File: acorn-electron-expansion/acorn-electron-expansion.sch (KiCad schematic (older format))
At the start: 11 parts, among them P1 Acorn Electron Expansion Conn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, P2 CONN_02X24, U1 74hct125d, U2 74LVC245 D0-7, U3 74LVC245 A0-7, U4 74LVC245 A8-15, U5 74LVC245

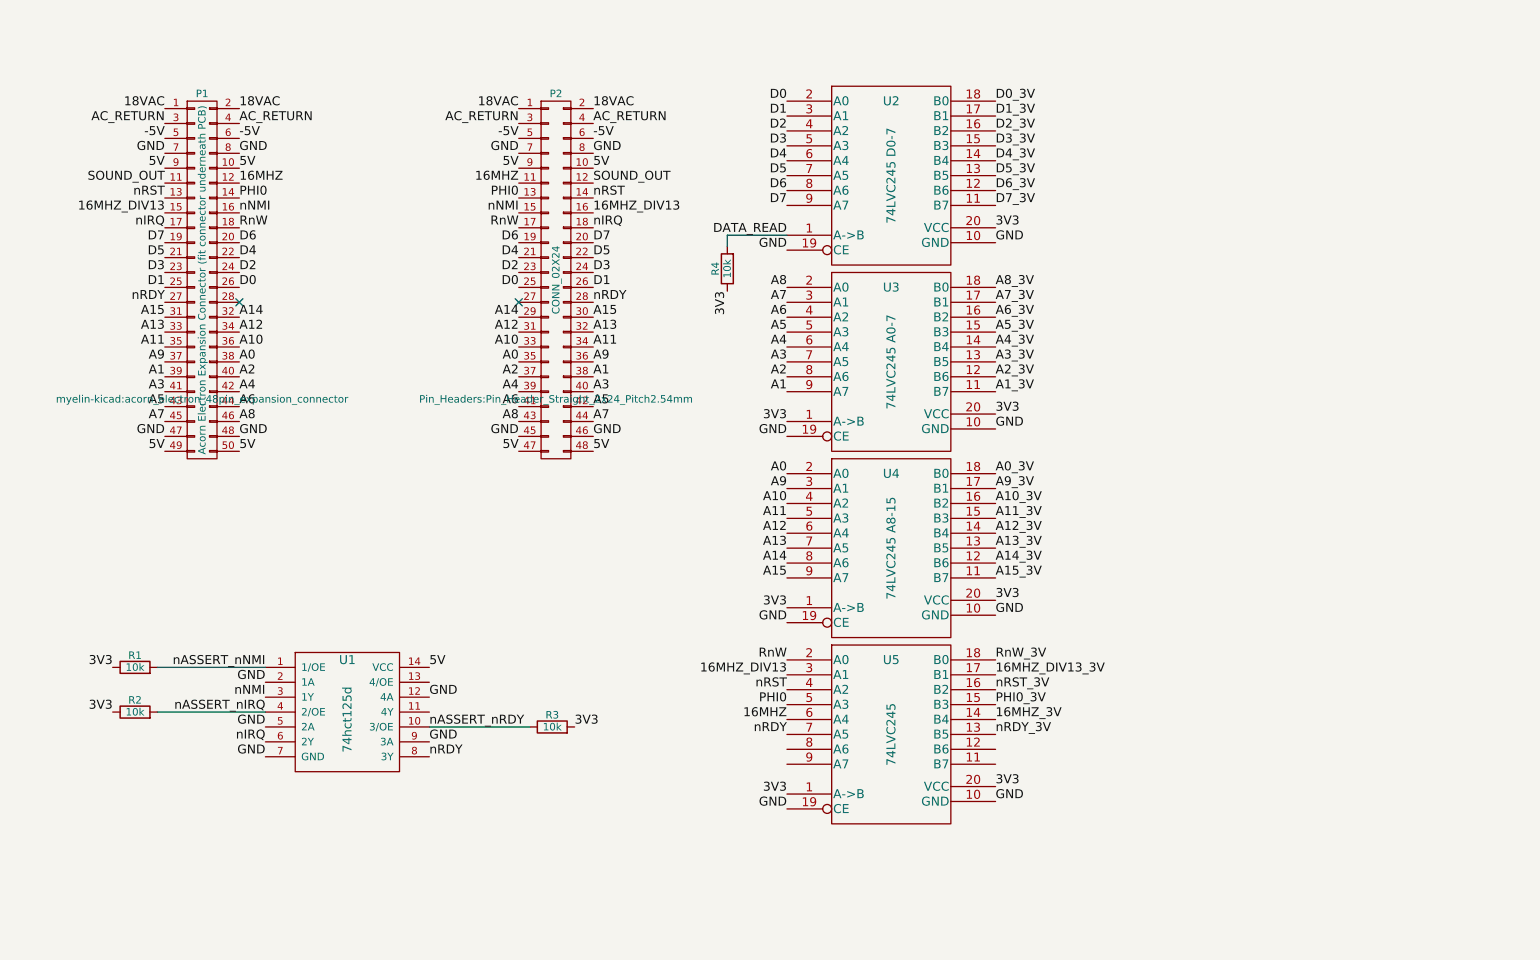
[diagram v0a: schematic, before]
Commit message: Made library and module for Scarab miniSpartan6+ board, and routed most of the level conversion stuff up top
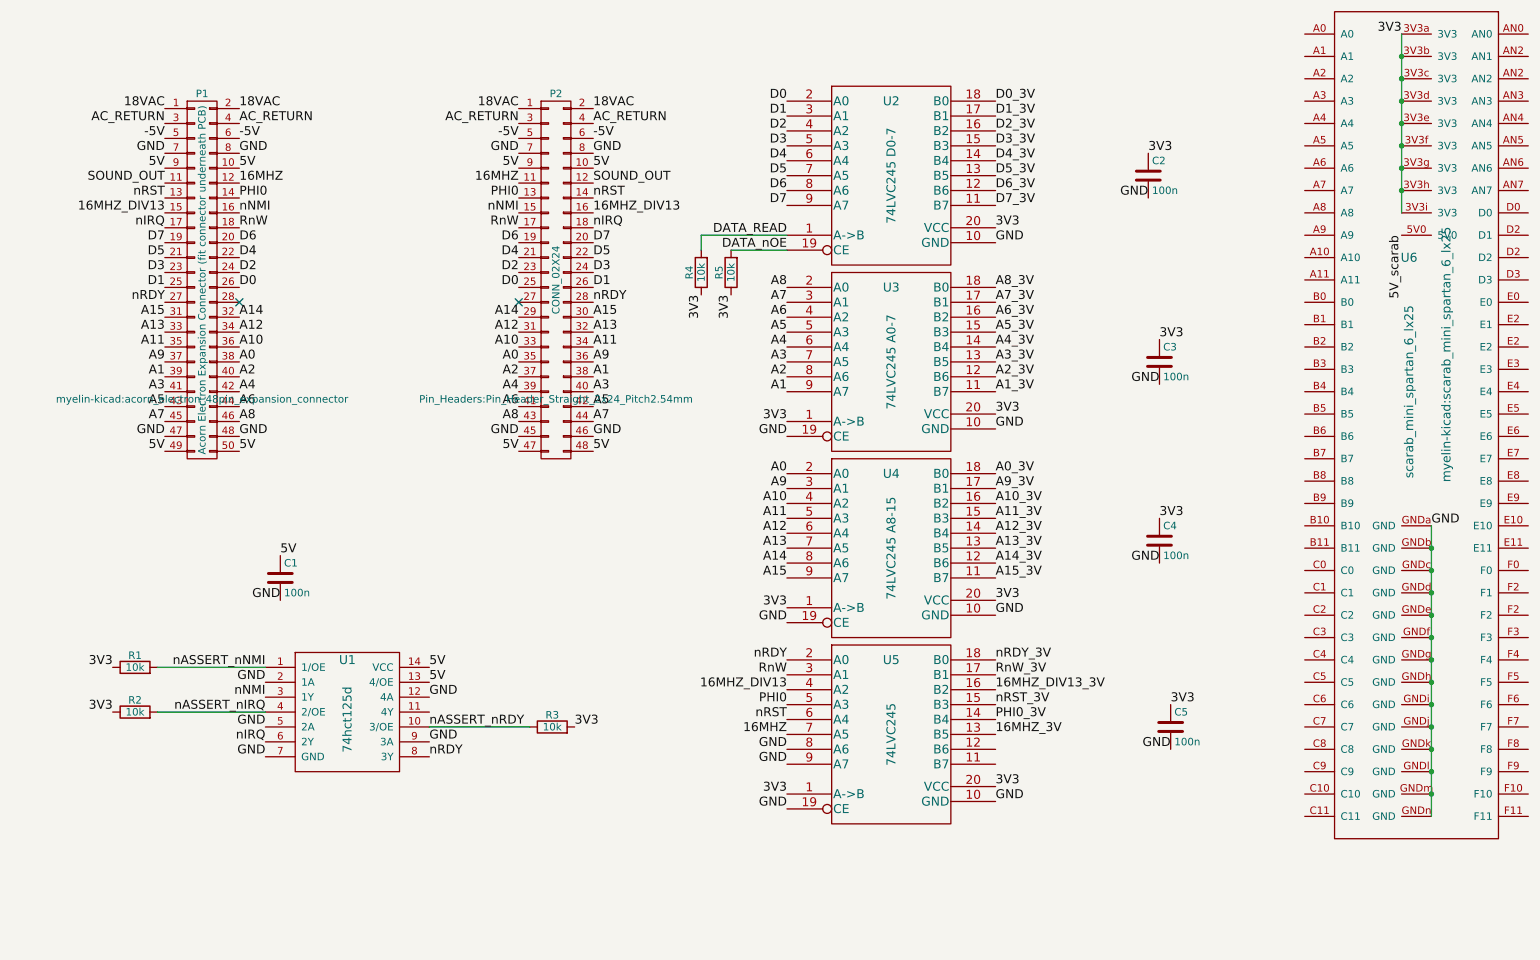
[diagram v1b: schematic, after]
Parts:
- added C1, C2, C3, C4, C5: 100n, myelin-kicad:C0805_nosilkscreen, symbol C0805
- added R5: 10k, myelin-kicad:R0805_nosilkscreen, symbol R0805
- added U6: scarab_mini_spartan_6_lx25, myelin-kicad:scarab_mini_spartan_6_lx25, symbol scarab_mini_spartan_6_lx25
- U2, U3, U4, U5: footprint Housings_SOIC:SOIC-20W_7.5x12.8mm_Pitch1.27mm -> Housings_SSOP:SSOP-20_4.4x6.5mm_Pitch0.65mm
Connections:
- net 16MHZ: now also U5.7 (A5); no longer U5.6 (A4)
- net 16MHZ_3V: now also U5.13 (B5); no longer U5.14 (B4)
- net 16MHZ_DIV13: now also U5.4 (A2); no longer U5.3 (A1)
- net 16MHZ_DIV13_3V: now also U5.16 (B2); no longer U5.17 (B1)
- net 3V3: now also C2.1, C3.1, C4.1, C5.1, R5.1, U6.3V3a (3V3), U6.3V3b (3V3), U6.3V3c (3V3), U6.3V3d (3V3), U6.3V3e (3V3), U6.3V3f (3V3), U6.3V3g (3V3), U6.3V3h (3V3), U6.3V3i (3V3)
- net 5V: now also U1.13 (4/OE), C1.1
- net GND: now also U5.8 (A6), U5.9 (A7), C1.2, C2.2, C3.2, C4.2, C5.2, U6.GNDa (GND), U6.GNDb (GND), U6.GNDc (GND), U6.GNDd (GND), U6.GNDe (GND), U6.GNDf (GND), U6.GNDg (GND), U6.GNDh (GND), U6.GNDi (GND), U6.GNDj (GND), U6.GNDk (GND), U6.GNDl (GND), U6.GNDm (GND), U6.GNDn (GND); no longer U2.19 (CE)
- net PHI0_3V: now also U5.14 (B4); no longer U5.15 (B3)
- net RnW: now also U5.3 (A1); no longer U5.2 (A0)
- net RnW_3V: now also U5.17 (B1); no longer U5.18 (B0)
- net nRDY: now also U5.2 (A0); no longer U5.7 (A5)
- net nRDY_3V: now also U5.18 (B0); no longer U5.13 (B5)
- net nRST: now also U5.6 (A4); no longer U5.4 (A2)
- net nRST_3V: now also U5.15 (B3); no longer U5.16 (B2)
- new net 5V_scarab: U6.5V0
- new net DATA_nOE: R5.2, U2.19 (CE)
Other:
- moved on the sheet: R4
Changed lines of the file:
@@
 LIBS:c0805
 LIBS:r0805
+LIBS:scarab_mini_spartan_6_lx25
+LIBS:acorn-electron-expansion-cache
 EELAYER 25 0
 EELAYER END
@@
 F 0 "U2" H 6300 2250 60  0000 C CNN
 F 1 "74LVC245 D0-7" V 6300 1750 60  0000 C CNN
-F 2 "Housings_SOIC:SOIC-20W_7.5x12.8mm_Pitch1.27mm" H 6300 1050 60  0001 C CNN
+F 2 "Housings_SSOP:SSOP-20_4.4x6.5mm_Pitch0.65mm" H 6300 1050 60  0001 C CNN
 F 3 "" H 6300 1750 60  0000 C CNN
 	1    6300 1750
@@
 F 0 "U3" H 6300 3500 60  0000 C CNN
 F 1 "74LVC245 A0-7" V 6300 3000 60  0000 C CNN
-F 2 "Housings_SOIC:SOIC-20W_7.5x12.8mm_Pitch1.27mm" H 6300 2300 60  0001 C CNN
+F 2 "Housings_SSOP:SSOP-20_4.4x6.5mm_Pitch0.65mm" H 6300 2300 60  0001 C CNN
 F 3 "" H 6300 3000 60  0000 C CNN
 	1    6300 3000
@@
 F 0 "U4" H 6300 4750 60  0000 C CNN
 F 1 "74LVC245 A8-15" V 6300 4250 60  0000 C CNN
-F 2 "Housings_SOIC:SOIC-20W_7.5x12.8mm_Pitch1.27mm" H 6300 3550 60  0001 C CNN
+F 2 "Housings_SSOP:SSOP-20_4.4x6.5mm_Pitch0.65mm" H 6300 3550 60  0001 C CNN
 F 3 "" H 6300 4250 60  0000 C CNN
 	1    6300 4250
@@
 F 0 "U5" H 6300 6000 60  0000 C CNN
 F 1 "74LVC245" V 6300 5500 60  0000 C CNN
-F 2 "Housings_SOIC:SOIC-20W_7.5x12.8mm_Pitch1.27mm" H 6300 4800 60  0001 C CNN
+F 2 "Housings_SSOP:SSOP-20_4.4x6.5mm_Pitch0.65mm" H 6300 4800 60  0001 C CNN
 F 3 "" H 6300 5500 60  0000 C CNN
 	1    6300 5500
@@
 Text Label 5600 4450 2    60   ~ 0
 A15
-Text Label 5600 5400 2    60   ~ 0
+Text Label 5600 5500 2    60   ~ 0
 16MHZ
 Text Label 5600 5300 2    60   ~ 0
 PHI0
+Text Label 5600 5200 2    60   ~ 0
+16MHZ_DIV13
 Text Label 5600 5100 2    60   ~ 0
-16MHZ_DIV13
-Text Label 5600 5000 2    60   ~ 0
 RnW
-Text Label 5600 5200 2    60   ~ 0
+Text Label 5600 5400 2    60   ~ 0
 nRST
 Text Label 2100 5250 2    60   ~ 0
@@
 Text Label 5600 6000 2    60   ~ 0
 GND
-Text Label 7000 5000 0    60   ~ 0
+Text Label 7000 5100 0    60   ~ 0
 RnW_3V
-Text Label 7000 5100 0    60   ~ 0
+Text Label 7000 5200 0    60   ~ 0
 16MHZ_DIV13_3V
-Text Label 7000 5200 0    60   ~ 0
+Text Label 7000 5300 0    60   ~ 0
 nRST_3V
-Text Label 7000 5300 0    60   ~ 0
+Text Label 7000 5400 0    60   ~ 0
 PHI0_3V
-Text Label 7000 5400 0    60   ~ 0
+Text Label 7000 5500 0    60   ~ 0
 16MHZ_3V
 Text Label 5600 5900 2    60   ~ 0
@@
 Text Label 5600 3400 2    60   ~ 0
 3V3
-Text Label 5600 2250 2    60   ~ 0
-GND
 $Comp
 L R0805 R4
 U 1 1 58D0D6B7
-P 5200 2375
-F 0 "R4" V 5280 2375 50  0000 C CNN
-F 1 "10k" V 5200 2375 50  0000 C CNN
-F 2 "myelin-kicad:R0805_nosilkscreen" V 5130 2375 50  0001 C CNN
-F 3 "" H 5200 2375 50  0000 C CNN
-	1    5200 2375
+P 5025 2400
+F 0 "R4" V 5105 2400 50  0000 C CNN
+F 1 "10k" V 5025 2400 50  0000 C CNN
+F 2 "myelin-kicad:R0805_nosilkscreen" V 4955 2400 50  0001 C CNN
+F 3 "" H 5025 2400 50  0000 C CNN
+	1    5025 2400
 	-1   0    0    1
 $EndComp
 Text Label 5600 2150 2    60   ~ 0
 DATA_READ
-Text Label 5200 2525 3    60   ~ 0
-3V3
-Wire Wire Line
-	5200 2225 5200 2150
-Wire Wire Line
-	5200 2150 5600 2150
+Text Label 5025 2550 3    60   ~ 0
+3V3
+Wire Wire Line
+	5025 2150 5600 2150
 Text Label 2100 5050 2    60   ~ 0
 nASSERT_nNMI
@@
 Text Label 4175 5450 0    60   ~ 0
 3V3
-Text Label 5600 5500 2    60   ~ 0
+Text Label 5600 5000 2    60   ~ 0
 nRDY
-Text Label 7000 5500 0    60   ~ 0
+Text Label 7000 5000 0    60   ~ 0
 nRDY_3V
+Text Label 5600 5600 2    60   ~ 0
+GND
+Text Label 5600 5700 2    60   ~ 0
+GND
+Text Label 3200 5150 0    60   ~ 0
+5V
+$Comp
+L C0805 C1
+U 1 1 58D21967
+P 2200 4450
+F 0 "C1" H 2225 4550 50  0000 L CNN
+F 1 "100n" H 2225 4350 50  0000 L CNN
+F 2 "myelin-kicad:C0805_nosilkscreen" H 2238 4300 50  0001 C CNN
+F 3 "" H 2200 4450 50  0000 C CNN
+	1    2200 4450
+	1    0    0    -1
+$EndComp
+Text Label 2200 4300 0    60   ~ 0
+5V
+Text Label 2200 4600 2    60   ~ 0
+GND
+Text Label 8025 1600 0    60   ~ 0
+3V3
+$Comp
+L C0805 C2
+U 1 1 58D21AC9
+P 8025 1750
+F 0 "C2" H 8050 1850 50  0000 L CNN
+F 1 "100n" H 8050 1650 50  0000 L CNN
+F 2 "myelin-kicad:C0805_nosilkscreen" H 8063 1600 50  0001 C CNN
+F 3 "" H 8025 1750 50  0000 C CNN
+	1    8025 1750
+	1    0    0    -1
+$EndComp
+Text Label 8025 1900 2    60   ~ 0
+GND
+Text Label 8100 2850 0    60   ~ 0
+3V3
+$Comp
+L C0805 C3
+U 1 1 58D21BC6
+P 8100 3000
+F 0 "C3" H 8125 3100 50  0000 L CNN
+F 1 "100n" H 8125 2900 50  0000 L CNN
+F 2 "myelin-kicad:C0805_nosilkscreen" H 8138 2850 50  0001 C CNN
+F 3 "" H 8100 3000 50  0000 C CNN
+	1    8100 3000
+	1    0    0    -1
+$EndComp
+Text Label 8100 3150 2    60   ~ 0
+GND
+Text Label 8100 4050 0    60   ~ 0
+3V3
+$Comp
+L C0805 C4
+U 1 1 58D21C56
+P 8100 4200
+F 0 "C4" H 8125 4300 50  0000 L CNN
+F 1 "100n" H 8125 4100 50  0000 L CNN
+F 2 "myelin-kicad:C0805_nosilkscreen" H 8138 4050 50  0001 C CNN
+F 3 "" H 8100 4200 50  0000 C CNN
+	1    8100 4200
+	1    0    0    -1
+$EndComp
+Text Label 8100 4350 2    60   ~ 0
+GND
+Text Label 8175 5300 0    60   ~ 0
+3V3
+$Comp
+L C0805 C5
+U 1 1 58D21C5E
+P 8175 5450
+F 0 "C5" H 8200 5550 50  0000 L CNN
+F 1 "100n" H 8200 5350 50  0000 L CNN
+F 2 "myelin-kicad:C0805_nosilkscreen" H 8213 5300 50  0001 C CNN
+F 3 "" H 8175 5450 50  0000 C CNN
+	1    8175 5450
+	1    0    0    -1
+$EndComp
+Text Label 8175 5600 2    60   ~ 0
+GND
+Text Label 5600 2250 2    60   ~ 0
+DATA_nOE
+Wire Wire Line
+	5025 2250 5025 2150
+$Comp
+L R0805 R5
+U 1 1 58D2266D
+P 5225 2400
+F 0 "R5" V 5305 2400 50  0000 C CNN
+F 1 "10k" V 5225 2400 50  0000 C CNN
+F 2 "myelin-kicad:R0805_nosilkscreen" V 5155 2400 50  0001 C CNN
+F 3 "" H 5225 2400 50  0000 C CNN
+	1    5225 2400
+	-1   0    0    1
+$EndComp
+Text Label 5225 2550 3    60   ~ 0
+3V3
+Wire Wire Line
+	5225 2250 5600 2250
+$Comp
+L scarab_mini_spartan_6_lx25 U6
+U 1 1 58D25E8C
+P 9775 4800
+F 0 "U6" H 9775 7300 60  0000 C CNN
+F 1 "scarab_mini_spartan_6_lx25" V 9775 6400 60  0000 C CNN
+F 2 "myelin-kicad:scarab_mini_spartan_6_lx25" V 10025 6650 60  0000 C CNN
+F 3 "" H 8825 4650 60  0000 C CNN
+	1    9775 4800
+	1    0    0    -1
+$EndComp
+Wire Wire Line
+	9925 4100 9925 6050
+Connection ~ 9925 4250
+Connection ~ 9925 4400
+Connection ~ 9925 4550
+Connection ~ 9925 4700
+Connection ~ 9925 4850
+Connection ~ 9925 5000
+Connection ~ 9925 5150
+Connection ~ 9925 5300
+Connection ~ 9925 5450
+Connection ~ 9925 5600
+Connection ~ 9925 5750
+Connection ~ 9925 5900
+Connection ~ 9725 950
+Connection ~ 9725 1100
+Connection ~ 9725 1250
+Connection ~ 9725 1400
+Connection ~ 9725 1550
+Connection ~ 9725 1700
+Connection ~ 9725 1850
+Text Label 9725 800  2    60   ~ 0
+3V3
+Text Label 9925 4100 0    60   ~ 0
+GND
+Wire Wire Line
+	9725 2000 9725 800
+Text Label 9725 2150 3    60   ~ 0
+5V_scarab
 $EndSCHEMATC

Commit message: Possibly final board... needs verification but almost ready to go to fab
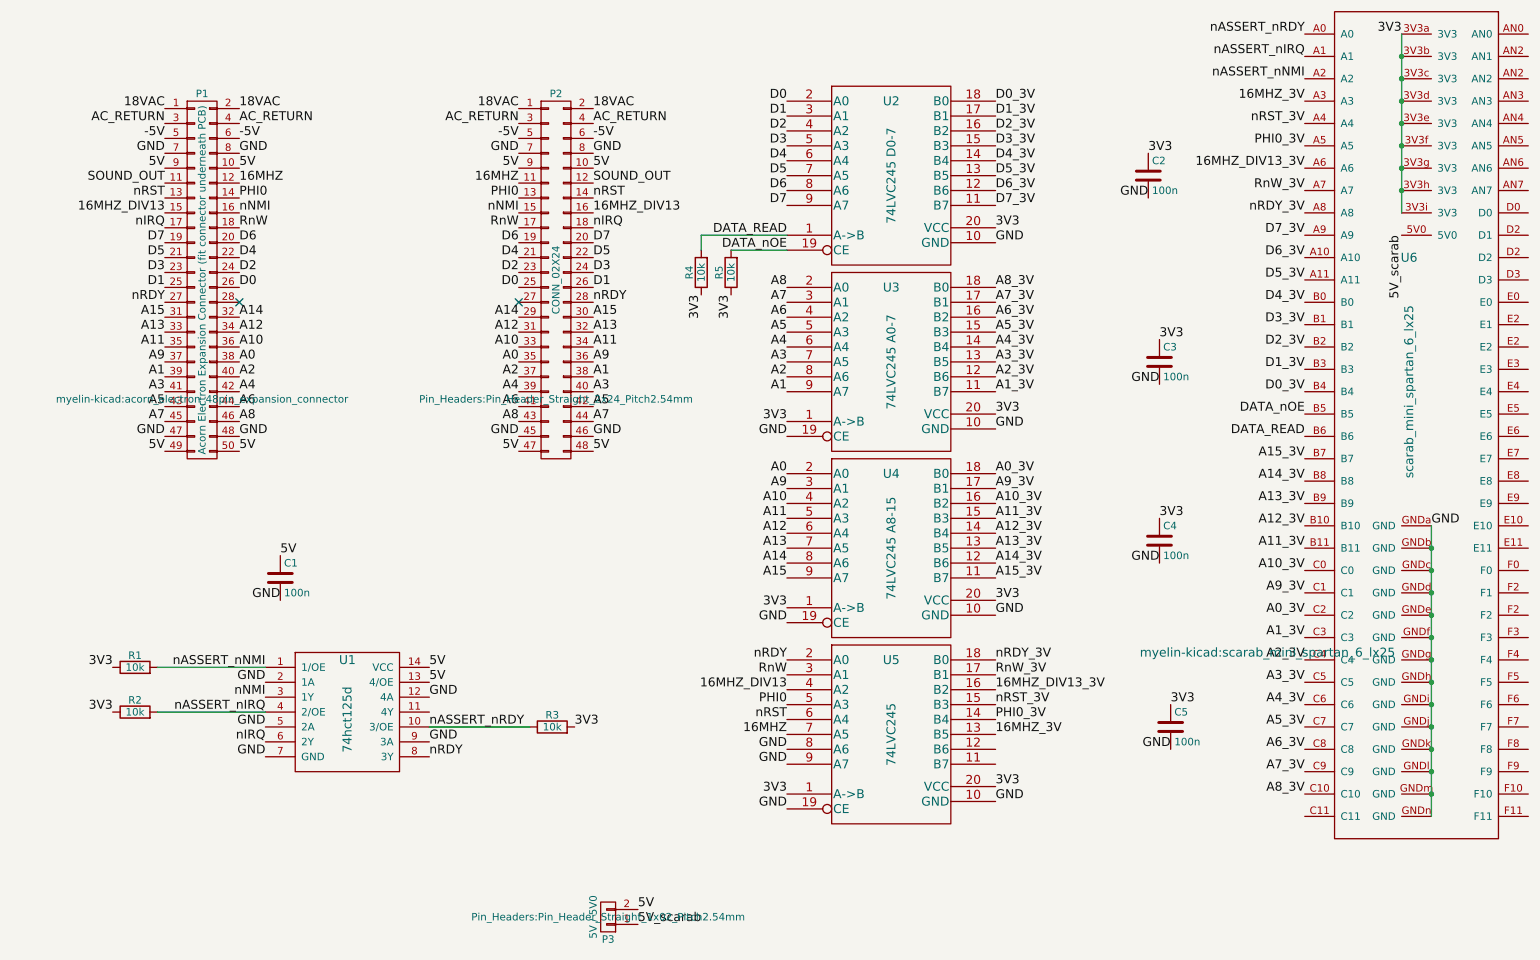
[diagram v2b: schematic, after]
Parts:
- added P3: 5V / 5V0, Pin_Headers:Pin_Header_Straight_1x02_Pitch2.54mm, symbol CONN_01X02
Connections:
- net 16MHZ_3V: now also U6.A3
- net 16MHZ_DIV13_3V: now also U6.A6
- net 5V: now also P3.2 (P2)
- net 5V_scarab: now also P3.1 (P1)
- net A0_3V: now also U6.C2
- net A10_3V: now also U6.C0
- net A11_3V: now also U6.B11
- net A12_3V: now also U6.B10
- net A13_3V: now also U6.B9
- net A14_3V: now also U6.B8
- net A15_3V: now also U6.B7
- net A1_3V: now also U6.C3
- net A2_3V: now also U6.C4
- net A3_3V: now also U6.C5
- net A4_3V: now also U6.C6
- net A5_3V: now also U6.C7
- net A6_3V: now also U6.C8
- net A7_3V: now also U6.C9
- net A8_3V: now also U6.C10
- net A9_3V: now also U6.C1
- net D0_3V: now also U6.B4
- net D1_3V: now also U6.B3
- net D2_3V: now also U6.B2
- net D3_3V: now also U6.B1
- net D4_3V: now also U6.B0
- net D5_3V: now also U6.A11
- net D6_3V: now also U6.A10
- net D7_3V: now also U6.A9
- net DATA_READ: now also U6.B6
- net DATA_nOE: now also U6.B5
- net PHI0_3V: now also U6.A5
- net RnW_3V: now also U6.A7
- net nASSERT_nIRQ: now also U6.A1
- net nASSERT_nNMI: now also U6.A2
- net nASSERT_nRDY: now also U6.A0
- net nRDY_3V: now also U6.A8
- net nRST_3V: now also U6.A4
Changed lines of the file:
@@
 F 0 "U6" H 9775 7300 60  0000 C CNN
 F 1 "scarab_mini_spartan_6_lx25" V 9775 6400 60  0000 C CNN
-F 2 "myelin-kicad:scarab_mini_spartan_6_lx25" V 10025 6650 60  0000 C CNN
+F 2 "myelin-kicad:scarab_mini_spartan_6_lx25" H 8825 4650 60  0000 C CNN
 F 3 "" H 8825 4650 60  0000 C CNN
 	1    9775 4800
@@
 Text Label 9725 2150 3    60   ~ 0
 5V_scarab
+Text Label 9075 800  2    60   ~ 0
+nASSERT_nRDY
+Text Label 9075 950  2    60   ~ 0
+nASSERT_nIRQ
+Text Label 9075 1100 2    60   ~ 0
+nASSERT_nNMI
+Text Label 9075 1850 2    60   ~ 0
+RnW_3V
+Text Label 9075 1700 2    60   ~ 0
+16MHZ_DIV13_3V
+Text Label 9075 1400 2    60   ~ 0
+nRST_3V
+Text Label 9075 1550 2    60   ~ 0
+PHI0_3V
+Text Label 9075 1250 2    60   ~ 0
+16MHZ_3V
+Text Label 9075 2000 2    60   ~ 0
+nRDY_3V
+Text Label 9075 3200 2    60   ~ 0
+D0_3V
+Text Label 9075 3050 2    60   ~ 0
+D1_3V
+Text Label 9075 2900 2    60   ~ 0
+D2_3V
+Text Label 9075 2750 2    60   ~ 0
+D3_3V
+Text Label 9075 2600 2    60   ~ 0
+D4_3V
+Text Label 9075 2450 2    60   ~ 0
+D5_3V
+Text Label 9075 2300 2    60   ~ 0
+D6_3V
+Text Label 9075 2150 2    60   ~ 0
+D7_3V
+Text Label 9075 3650 2    60   ~ 0
+A15_3V
+Text Label 9075 3800 2    60   ~ 0
+A14_3V
+Text Label 9075 3950 2    60   ~ 0
+A13_3V
+Text Label 9075 4100 2    60   ~ 0
+A12_3V
+Text Label 9075 4250 2    60   ~ 0
+A11_3V
+Text Label 9075 4400 2    60   ~ 0
+A10_3V
+Text Label 9075 4550 2    60   ~ 0
+A9_3V
+Text Label 9075 4700 2    60   ~ 0
+A0_3V
+Text Label 9075 3350 2    60   ~ 0
+DATA_nOE
+Text Label 9075 3500 2    60   ~ 0
+DATA_READ
+Text Label 9075 5900 2    60   ~ 0
+A8_3V
+Text Label 9075 5750 2    60   ~ 0
+A7_3V
+Text Label 9075 5600 2    60   ~ 0
+A6_3V
+Text Label 9075 5450 2    60   ~ 0
+A5_3V
+Text Label 9075 5300 2    60   ~ 0
+A4_3V
+Text Label 9075 5150 2    60   ~ 0
+A3_3V
+Text Label 9075 5000 2    60   ~ 0
+A2_3V
+Text Label 9075 4850 2    60   ~ 0
+A1_3V
+Text Label 4600 6775 0    60   ~ 0
+5V_scarab
+Text Label 4600 6675 0    60   ~ 0
+5V
+$Comp
+L CONN_01X02 P3
+U 1 1 58D25ACD
+P 4400 6725
+F 0 "P3" H 4400 6875 50  0000 C CNN
+F 1 "5V / 5V0" V 4500 6725 50  0000 C CNN
+F 2 "Pin_Headers:Pin_Header_Straight_1x02_Pitch2.54mm" H 4400 6725 50  0000 C CNN
+F 3 "" H 4400 6725 50  0000 C CNN
+	1    4400 6725
+	-1   0    0    1
+$EndComp
 $EndSCHEMATC
